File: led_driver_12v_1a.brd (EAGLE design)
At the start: 97.4 x 49.5 mm, 35 parts, among them Q1 BSZ0902NSI, Q2 BSZ0902NSI, Q3 BSZ0902NSI, Q4 BSZ0902NSI, Q5 BSZ0902NSI

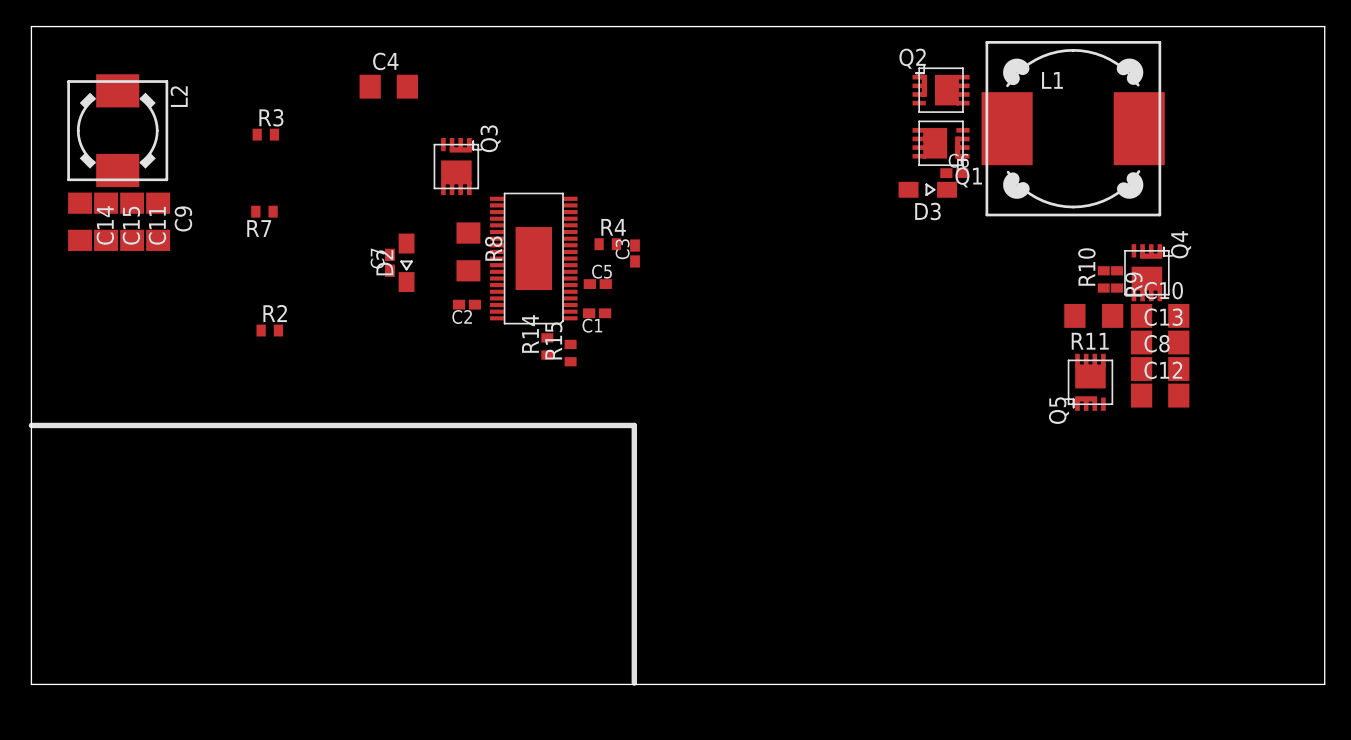
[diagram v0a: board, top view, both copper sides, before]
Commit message: schematics roughly finished, components are roughly in place. Need accurate routing and fine component adjustments
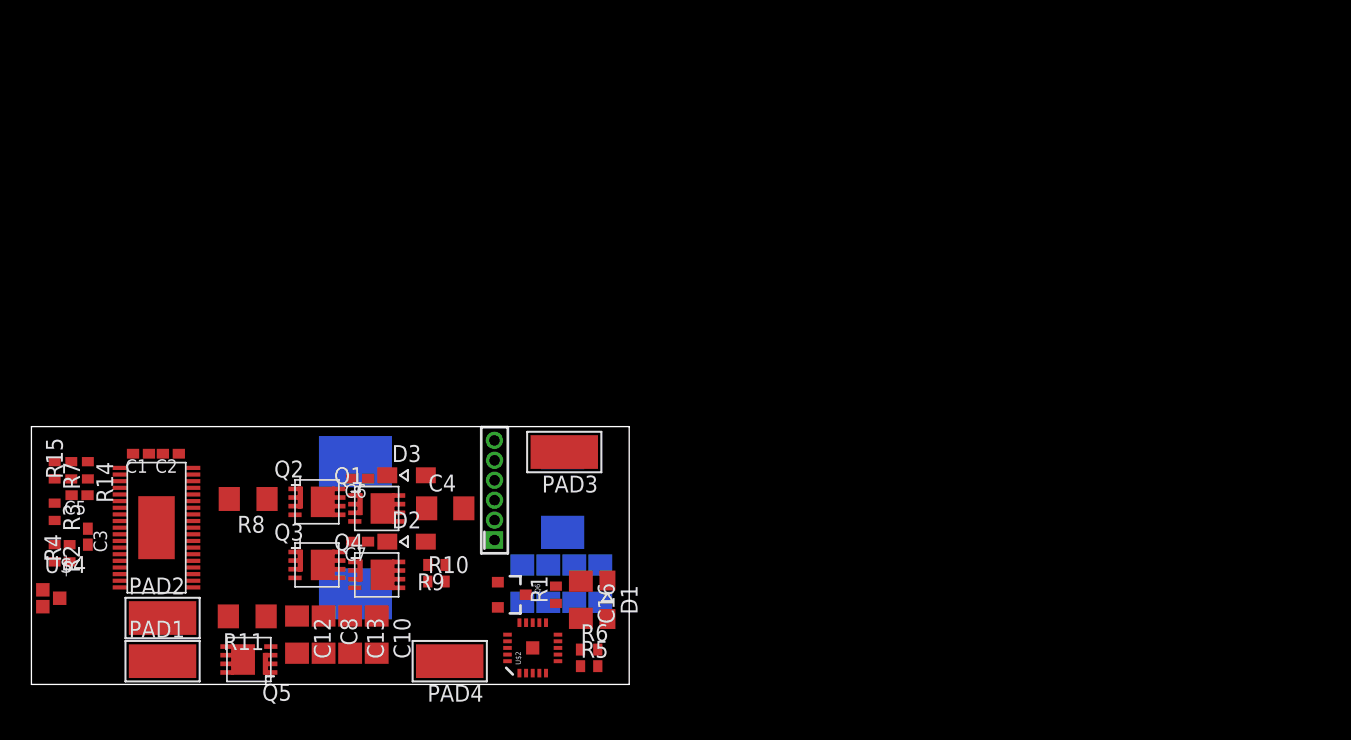
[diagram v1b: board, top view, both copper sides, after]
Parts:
- added C16: 4.7uF, 25V, Low ESR (Kemet C1206C475K3RACTU), rcl:C1206
- added D1: BAT46-WJ, diode:SOD323-W
- added PAD1: LED-, wirepad:5-2,5
- added PAD2, PAD3, PAD4: LED+, wirepad:5-2,5
- added Q6: SSM3K2615R, SparkFun-DiscreteSemi:SOT23-3
- added R1: 10k, resistor:R0402
- added R5: 100k, resistor:R0402
- added R6: 56.9k, resistor:R0402
- added U$2: ATTINY24QFN, SparkFun-DigitalIC:QFN20
- added U$3: AVR_MINI_PROGSMD, SparkFun-Connectors:AVR_MINI_PROG
- added U$4: GND_CONNECT, SparkFun-Passives:GND_CONNECT
- moved R11 67.6 mm to (16.2, 5.12)
- moved C12 67.4 mm to (20.0, 3.75), turned to 270 degrees
- moved Q5 66.7 mm to (16.4, 1.88), turned to 180 degrees
- moved C8 66.1 mm to (22.0, 3.75), turned to 270 degrees
- moved C13 64.8 mm to (24.0, 3.75), turned to 270 degrees
- moved C10 63.7 mm to (26.0, 3.75), turned to 270 degrees
- moved Q4 62.3 mm to (26.0, 8.25), turned to 0 degrees
- moved L1 61.8 mm to (24.4, 11.8), flipped to the bottom, turned to 270 degrees
- moved Q2 56.3 mm to (21.5, 13.8)
- moved R9 55.6 mm to (30.5, 9.00), turned to 180 degrees
- moved R10 55.2 mm to (30.5, 7.75), turned to 0 degrees
- moved Q1 50.6 mm to (26.0, 13.2), turned to 0 degrees
- moved C6 50.3 mm to (24.8, 15.5), turned to 180 degrees
- moved C14 47.7 mm to (42.8, 7.59), flipped to the bottom
- moved R4 46.7 mm to (2.88, 9.88), turned to 90 degrees
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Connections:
- new net N$12: C16.1, D1.C, R1.1, U$2.9, U$3.1
- new net N$13: Q6.3, R1.2, U$2.14
- new net N$14: U$1.P$3, U$2.15
- new net N$15: R5.2, R6.1, U$2.5
- new net N$16: U$2.20, U$3.6
- new net N$17: U$2.16, U$3.4
- new net N$18: U$2.13, U$3.3
- new net N$19: PAD1.1, Q5.D, Q5.D@1, Q5.D@2, Q5.D@3, Q5.D@4
- new net N$20: U$2.1, U$3.5
- new net N$21: L2.1, PAD3.1
- net +12V: now also Q6.1, R5.1
- net DGND: now also C1.1, C16.2, Q6.2, R6.2, U$2.0, U$2.8, U$3.2, U$4.1
- net GND: now also PAD4.1, U$4.2, U$4.3; no longer C1.1
- net INTVCC: now also D1.A, U$1.P$32
- net ISN: now also PAD2.1
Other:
- board size 97.4 x 49.5 mm -> 45 x 19.4 mm

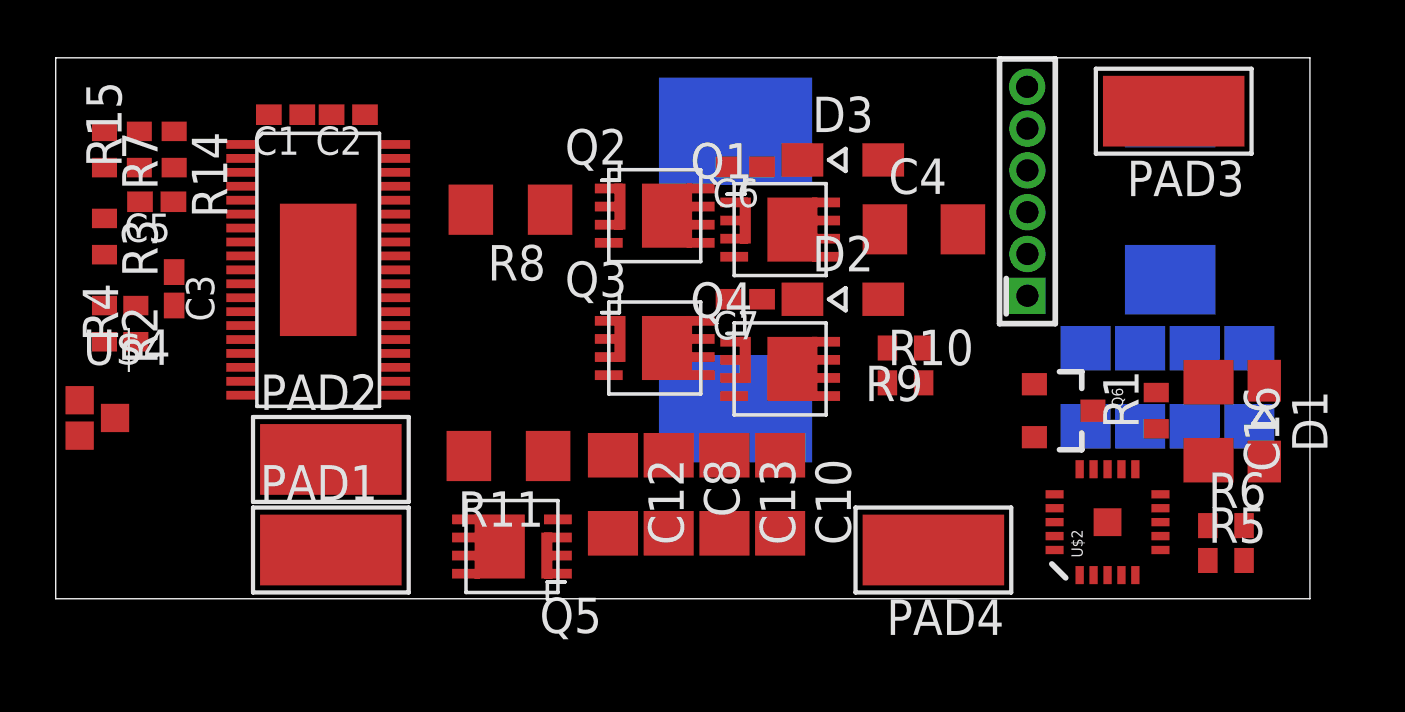
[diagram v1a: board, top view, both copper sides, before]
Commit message: second iteration of component placement. already have routing improvements, but still plenty of work to do
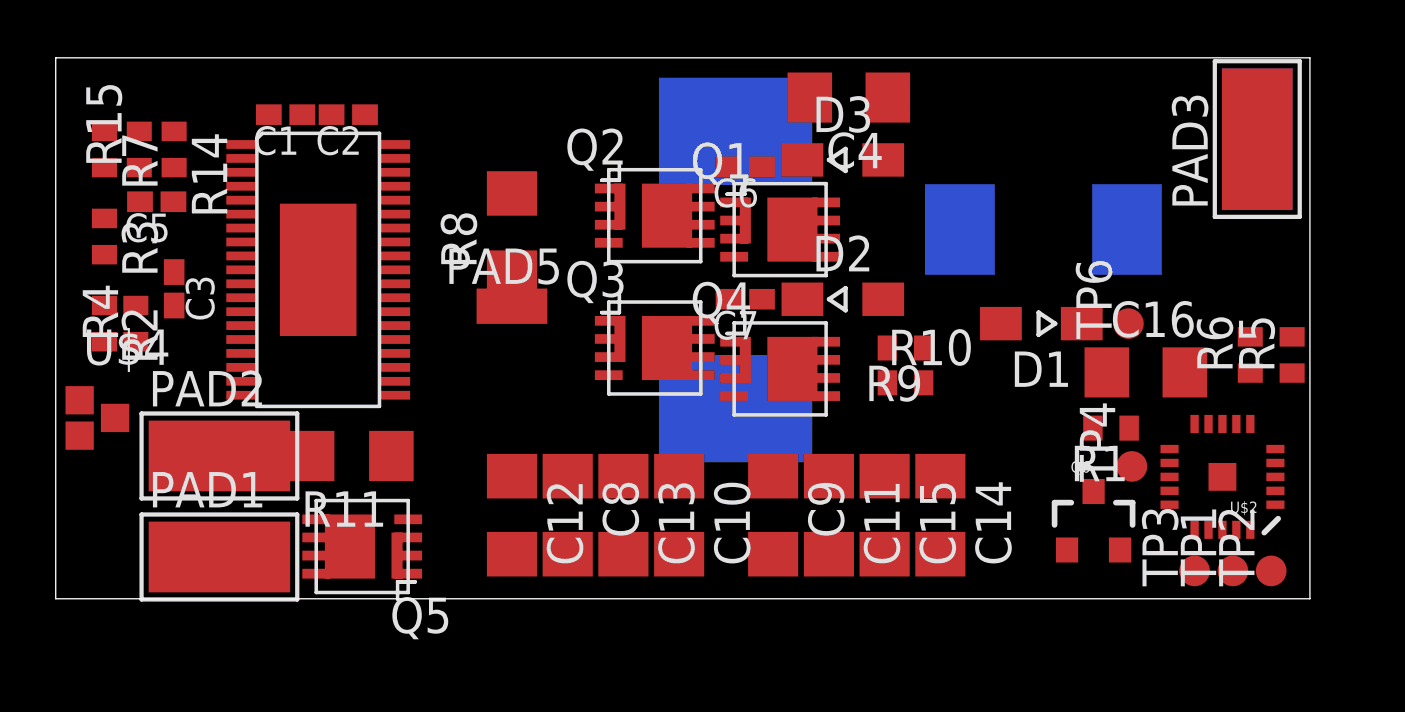
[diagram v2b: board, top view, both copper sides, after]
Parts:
- removed U$3: AVR_MINI_PROGSMD, SparkFun-Connectors:AVR_MINI_PROG
- added PAD5: GND, wirepad:SMD1,27-2,54
- added TP1, TP2, TP3, TP4, TP6: TPTP11R, testpad:TP11R
- moved PAD4 18.8 mm to (43.1, 16.5), flipped to the bottom, turned to 180 degrees
- moved C9 12.1 mm to (25.8, 3.00), flipped to the top
- moved C11 12.1 mm to (27.8, 3.00), flipped to the top
- moved C15 12.0 mm to (29.8, 3.00), flipped to the top
- moved C14 12.0 mm to (31.8, 3.00), flipped to the top
- moved D1 8.73 mm to (35.4, 9.88), turned to 180 degrees
- moved R5 7.75 mm to (44.4, 8.75), turned to 90 degrees
- moved R6 6.19 mm to (42.9, 8.75), turned to 90 degrees
- moved R11 5.62 mm to (10.6, 5.12)
- moved C4 5.44 mm to (28.5, 18.0), turned to 180 degrees
- moved Q5 5.38 mm to (11.0, 1.88)
- moved L2 4.71 mm to (35.5, 13.2), turned to 0 degrees
- moved U$2 4.43 mm to (41.9, 4.38), turned to 180 degrees
- moved Q6 4.16 mm to (37.2, 2.75), turned to 0 degrees
- moved PAD1 4.01 mm to (5.88, 1.50)
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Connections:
- net DGND: no longer U$3.2
- net GND: now also PAD5.1
- net N$12: now also TP6.TP; no longer U$3.1
- net N$16: now also TP1.TP; no longer U$3.6
- net N$17: now also TP3.TP; no longer U$3.4
- net N$18: now also TP4.TP; no longer U$3.3
- net N$20: now also TP2.TP; no longer U$3.5

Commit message: routing complete. main tasks to do: add polys, optimize routes width, add some extra vias, make gerbers
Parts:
- moved PAD4 24.2 mm to (24.0, 1.62), flipped to the top, turned to 90 degrees
- moved TP6 4.61 mm to (35.5, 6.38)
- moved PAD5 3.62 mm to (16.4, 14.1)
- moved PAD3 3.31 mm to (42.5, 13.2)
- moved D1 2.35 mm to (34.4, 7.75)
- moved R8 1.79 mm to (16.8, 11.4), turned to 270 degrees
- moved C10 1.50 mm to (20.9, 3.00)
- moved C12 1.50 mm to (14.9, 3.00)
- moved C13 1.50 mm to (18.9, 3.00)
- moved C8 1.50 mm to (16.9, 3.00)
- moved C11 1.38 mm to (29.1, 3.00)
- moved C14 1.38 mm to (33.1, 3.00)
- moved C15 1.38 mm to (31.1, 3.00)
- moved C9 1.38 mm to (27.1, 3.00)
- moved L1 1.38 mm to (24.4, 10.4)
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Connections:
- removed net N$10: C7.2, L1.2, Q3.D, Q3.D@1, Q3.D@2, Q3.D@3, Q3.D@4, Q4.S@1, Q4.S@2, Q4.S@3, Q4.S@4
- removed net N$8: C6.2, L1.1, Q1.S@1, Q1.S@2, Q1.S@3, Q1.S@4, Q2.D, Q2.D@1, Q2.D@2, Q2.D@3, Q2.D@4
- net SNSN: now also R8.1; no longer R8.2
- net SNSP: now also R8.2; no longer R8.1
- net SW1: now also C6.2, L1.1, Q1.S@1, Q1.S@2, Q1.S@3, Q1.S@4, Q2.D, Q2.D@1, Q2.D@2, Q2.D@3, Q2.D@4
- net SW2: now also C7.2, L1.2, Q3.D, Q3.D@1, Q3.D@2, Q3.D@3, Q3.D@4, Q4.S@1, Q4.S@2, Q4.S@3, Q4.S@4
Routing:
- net +12V: track 0.00 -> 104.3 mm, vias 0 -> 4
- net DGND: track 0.00 -> 95.2 mm, vias 0 -> 2
- net GND: track 0.00 -> 90.8 mm, vias 0 -> 5
- net INTVCC: track 0.00 -> 50.8 mm, vias 0 -> 2
- net N$14: track 0.00 -> 49.6 mm, vias 0 -> 2
- net N$6: track 0.00 -> 34.2 mm, vias 0 -> 2
- net SW1: track 0.00 -> 32.4 mm, vias 0 -> 2
- net ISP: track 0.00 -> 31.2 mm
- net SW2: track 0.00 -> 29.5 mm, vias 0 -> 5
- net BST1: track 0.00 -> 25.8 mm, vias 0 -> 2
- net PWMOUT: track 0.00 -> 21.3 mm, vias 0 -> 2
- net TG1: track 0.00 -> 20.5 mm, vias 0 -> 2
- net SNSP: track 0.00 -> 18.5 mm
- net BST2: track 0.00 -> 18.1 mm, vias 0 -> 2
- net BG1: track 0.00 -> 17.3 mm, vias 0 -> 2
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- added copper zone on layer 1, net SNSP

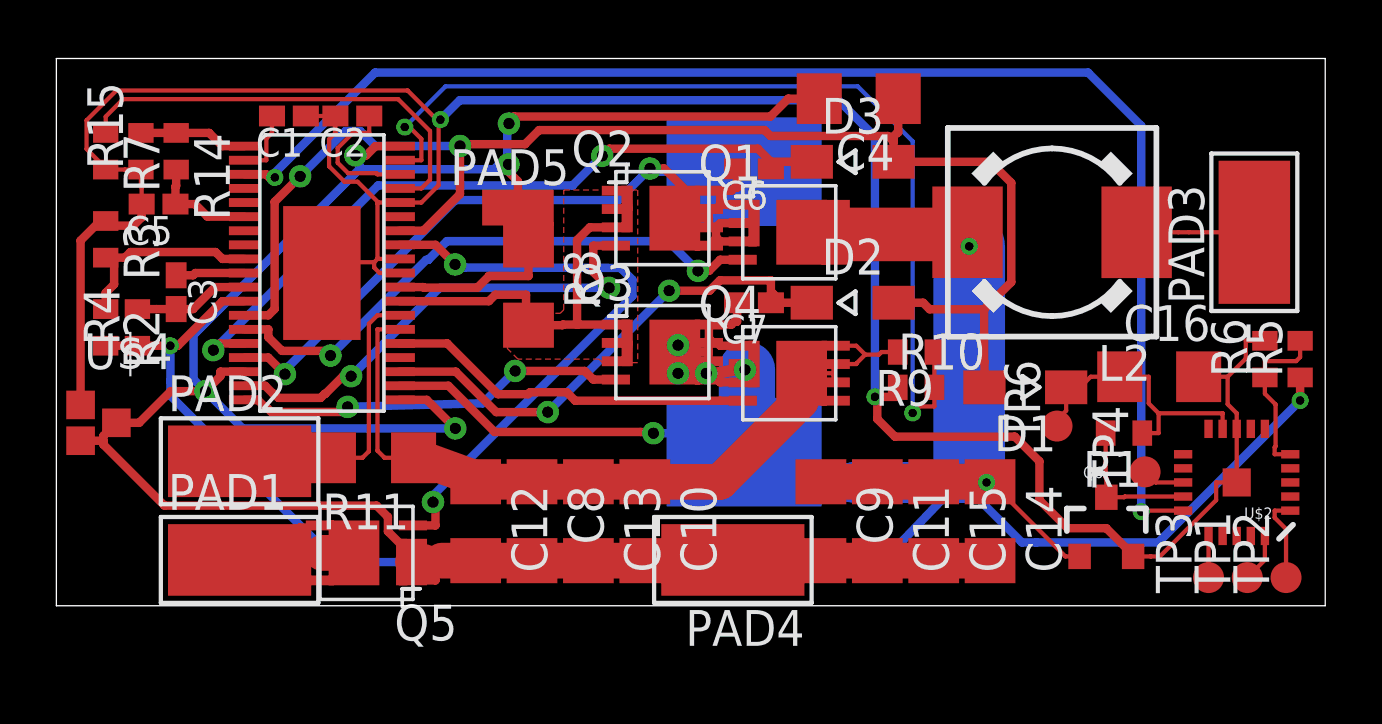
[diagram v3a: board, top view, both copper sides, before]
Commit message: added poly's & some traces optimization. Need to pretify silkscreen, check everything and make gerbers
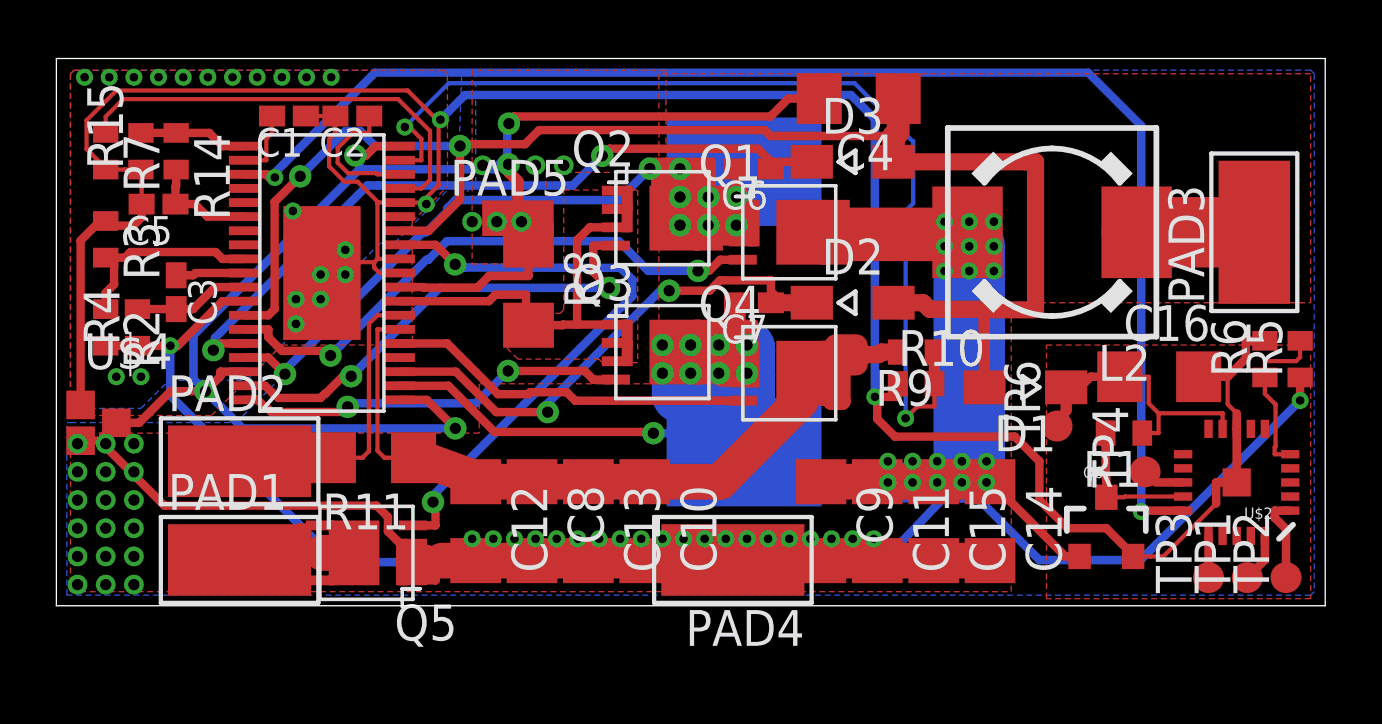
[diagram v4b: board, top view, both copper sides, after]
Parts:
- moved PAD5 0.38 mm to (16.4, 13.8)
- moved R10 0.12 mm to (30.5, 7.88)
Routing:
- net SW1: track 32.4 -> 63.9 mm, vias 2 -> 9
- net SW2: track 29.5 -> 57.6 mm, vias 5 -> 9
- net +12V: track 104.3 -> 108.2 mm, vias 4 -> 21
- net ISP: track 31.2 -> 34.9 mm
- net INTVCC: track 50.8 -> 53.7 mm
- net N$6: track 34.2 -> 34.9 mm
- net DGND: track 95.2 -> 95.9 mm, vias 2 -> 23
- net GND: track 90.8 -> 91.2 mm, vias 5 -> 49
- added copper zone on layer 1, net DGND
- added copper zone on layer 16, net DGND
- added copper zone on layer 1, net GND
- added copper zone on layer 16, net GND

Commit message: Added Gerbers and PartList
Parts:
- C16, C4: value 4.7uF, 25V, Low ESR (Kemet C1206C475K3RACTU) -> 4.7uF
- renumbered TP1 to MISO, TP2 to SCK, TP3 to MOSI, TP4 to RST, TP6 to VCC
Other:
- board text added: "C1,C2 22nF (0402) C3 470nF (0402) C5,C6,C7 0.1uF (0402) C4,C8-C16 4.7uF (Kemet C1206C475K3RACTU)"
- board text added: "D1"
- board text added: "D1-D3 BAT46-WJ L1 4.7u (744771004) L2 1000n (Bourns Inc. SRR7045-1R0M) Q1-Q5 BSZ0902NSI Q6 SSM3K2615R U1 LT3791 TSSOP38 U2 ATTINY24A (QFN)"
- board text added: "IN: LiPo 3S OUT: 12V/1.05A"
- board text added: "R4 50(0402) R1 10k(0402) R3,R6,R15 56.9k(0402) R7,R10 86.6k(0402) R5,R14 100k(0402) R2 300k(0402) R9 1Meg(0402) R8 10m(1206) Riedon CSR1206-0R001F1 R11 50m(1206) Ohmite MCS1632R005FER"
- board text added: "U1"
- board text added: "U2"
